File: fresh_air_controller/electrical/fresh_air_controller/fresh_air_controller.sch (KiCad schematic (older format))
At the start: 30 parts, among them J1 Screw_Terminal_01x02, J2 Screw_Terminal_01x02, J3 Screw_Terminal_01x12, J4 Screw_Terminal_01x12, J5 Conn_01x10_MountingPin, K1 FINDER-34.51, K2 FINDER-34.51, K3 FINDER-34.51, K4 FINDER-34.51, U1 DHT11, U2 DHT11, U3 DHT11, U4 esp32-gateway, U5 AC_DC_PWR_REG, U6 DC_DC_PWR_REG, U7 PCF8574A

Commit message: updates.
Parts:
- removed J1, J2: Screw_Terminal_01x02, symbol Connector:Screw_Terminal_01x02
- removed J3, J4: Screw_Terminal_01x12, symbol Connector:Screw_Terminal_01x12
- removed J5: Conn_01x10_MountingPin, symbol Connector_Generic_MountingPin:Conn_01x10_MountingPin
- removed J?: Screw_Terminal_01x03, symbol Connector:Screw_Terminal_01x03
- removed K1, K2, K3, K4, K?: FINDER-34.51, Relay_THT:Relay_SPDT_Finder_34.51_Vertical, symbol Relay:FINDER-34.51
- removed R1, R2: R, symbol Device:R
- removed R? (x5): 3K3, symbol Device:R
- removed U1, U2, U3: DHT11, Sensor:Aosong_DHT11_5.5x12.0_P2.54mm, symbol Sensor:DHT11
- removed U4: esp32-gateway, symbol birkler_comp:esp32-gateway
- removed U5: AC_DC_PWR_REG, symbol birkler_comp:AC_DC_PWR_REG
- removed U6: DC_DC_PWR_REG, symbol birkler_comp:DC_DC_PWR_REG
- removed U7: PCF8574A, symbol Interface_Expansion:PCF8574A
- removed U? (x5): ILQ74, symbol Isolator:ILQ74
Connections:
- net labels added: Damper
- net labels removed: +12V, +3V3, +5V, 3V3, AC, CIRC_FAN_IN, CIRC_FAN_OUT, COOL_INHIBIT, COOL_STAGE_1_COMPRESSOR_IN, COOL_STAGE_1_COMPRESSOR_OUT, COOL_STAGE_2, CT_NEG, CT_POS, CT_SHIELD, Earth, GND, HEAT_STAGE_1_THERM_IN, HEAT_STAGE_1_THERM_OUT, HEAT_STAGE_2, I2C_SCA, I2C_SCL, MOTOR_NEG, MOTOR_POS, NC1, NC2, SWT_DAMPER_CLOSED, SWT_DAMPER_OPENED, TEMP_COND_AIR, TEMP_FRESH_AIR, TEMP_INSIDE_AIR
- wire segments 199 -> 103
- no-connect marks 3 -> 0

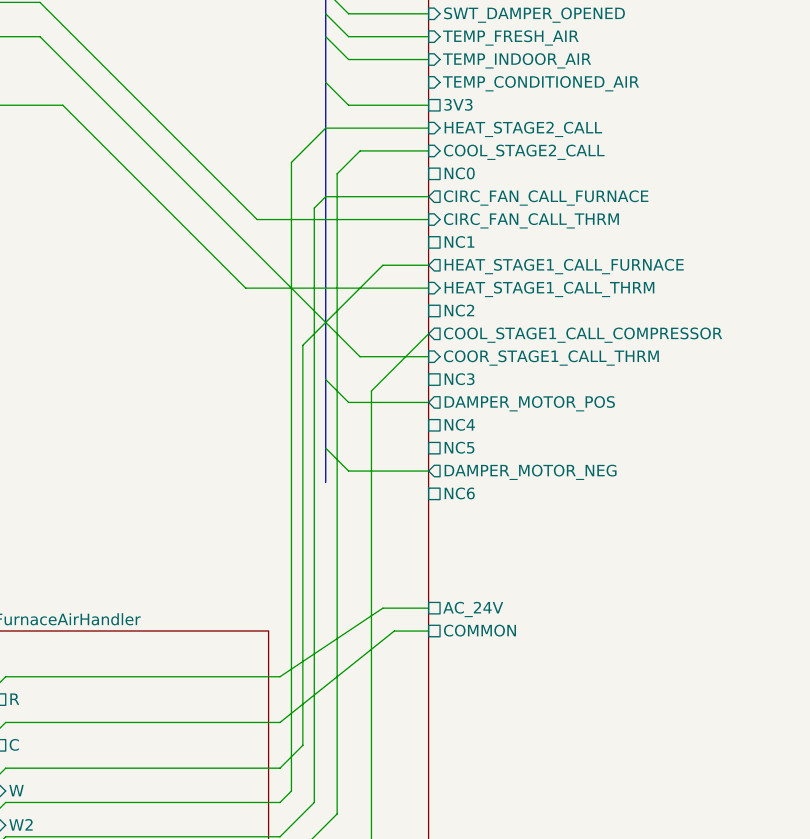
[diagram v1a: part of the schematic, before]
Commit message: use analog_threshold for monitor and garage doors. update some pinout for fresh air controller.
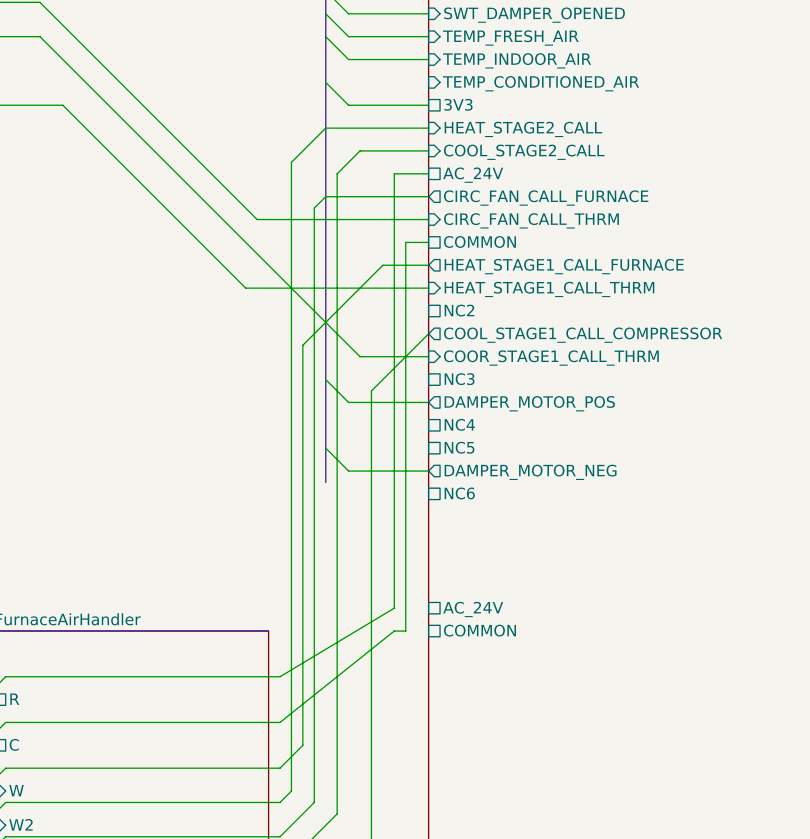
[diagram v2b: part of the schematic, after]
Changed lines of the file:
@@
 F22 "AC_24V" U L 8250 4000 50
 F23 "COMMON" U L 8250 4100 50
-F24 "NC0" U L 8250 2100 50
-F25 "NC1" U L 8250 2400 50
+F24 "AC_24V" U L 8250 2100 50
+F25 "COMMON" U L 8250 2400 50
 F26 "NC2" U L 8250 2700 50
 F27 "NC3" U L 8250 3000 50
@@
 	6400 4300 7600 4300
 Wire Wire Line
-	7600 4300 8050 4000
-Wire Wire Line
-	8050 4000 8250 4000
+	7600 4300 8100 4000
 Connection ~ 6300 4400
 Wire Wire Line
@@
 Wire Wire Line
 	7600 4500 8100 4100
-Wire Wire Line
-	8100 4100 8250 4100
 Connection ~ 6300 4600
 Wire Wire Line
@@
 Wire Wire Line
 	7900 3400 8250 3400
+Text Label 7000 700  0    50   ~ 0
+Damper
+Wire Wire Line
+	8100 2100 8250 2100
+Wire Wire Line
+	8100 2100 8100 4000
+Wire Wire Line
+	8100 4100 8150 4100
+Wire Wire Line
+	8150 4100 8150 2400
+Wire Wire Line
+	8150 2400 8250 2400
 Wire Bus Line
 	7800 800  7800 3450
-Text Label 7000 700  0    50   ~ 0
-Damper
 $EndSCHEMATC
